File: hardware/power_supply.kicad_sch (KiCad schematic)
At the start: 19 parts, among them U4 LM5164DDA, U5 AP7361-33E

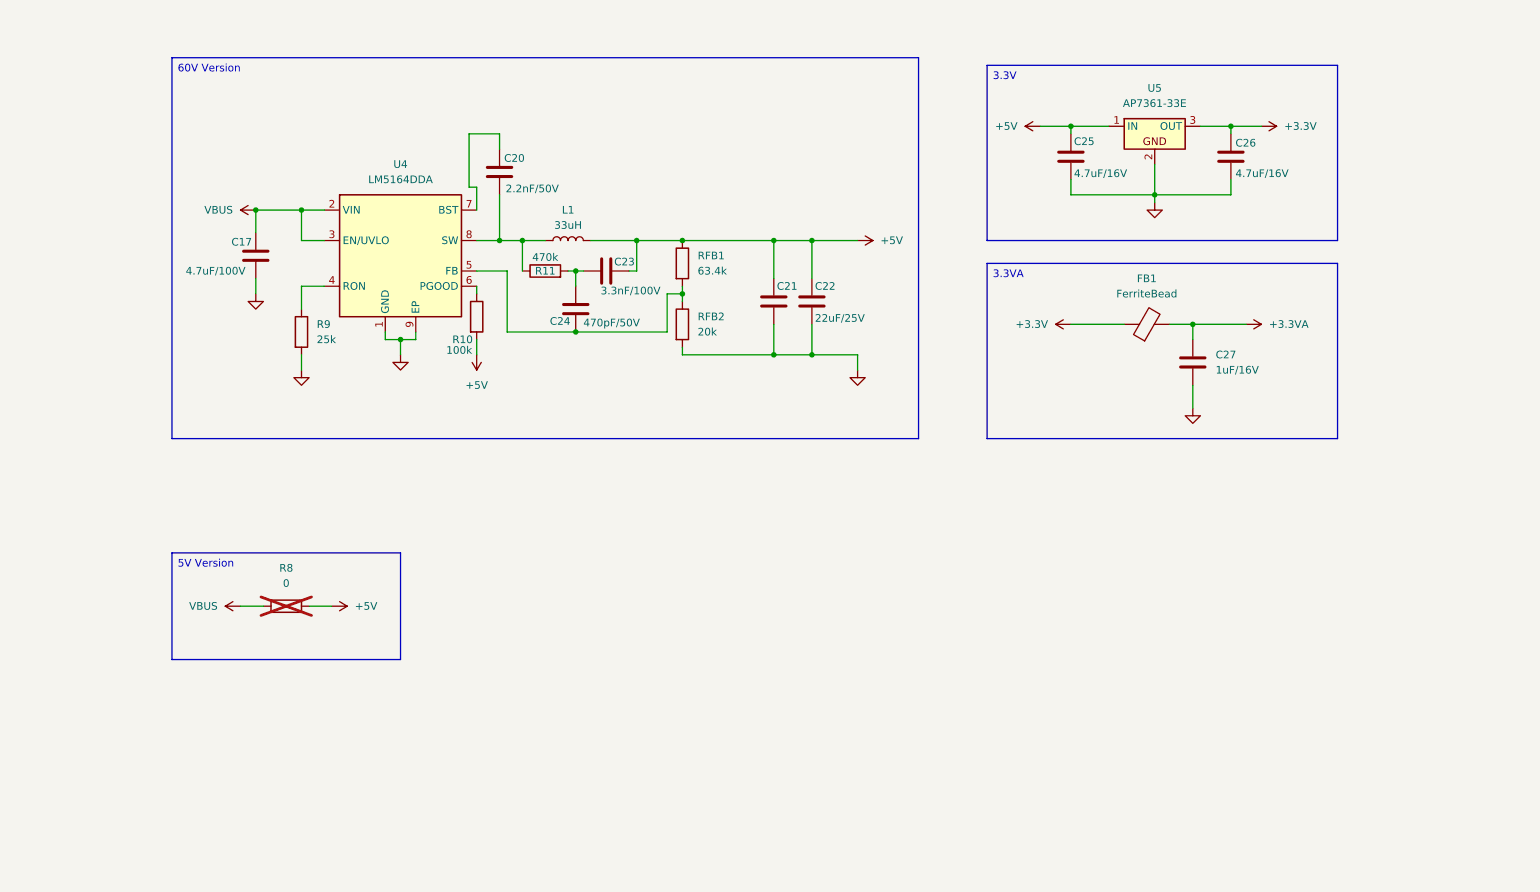
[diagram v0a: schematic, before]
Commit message: ✨ Further power supply schematic
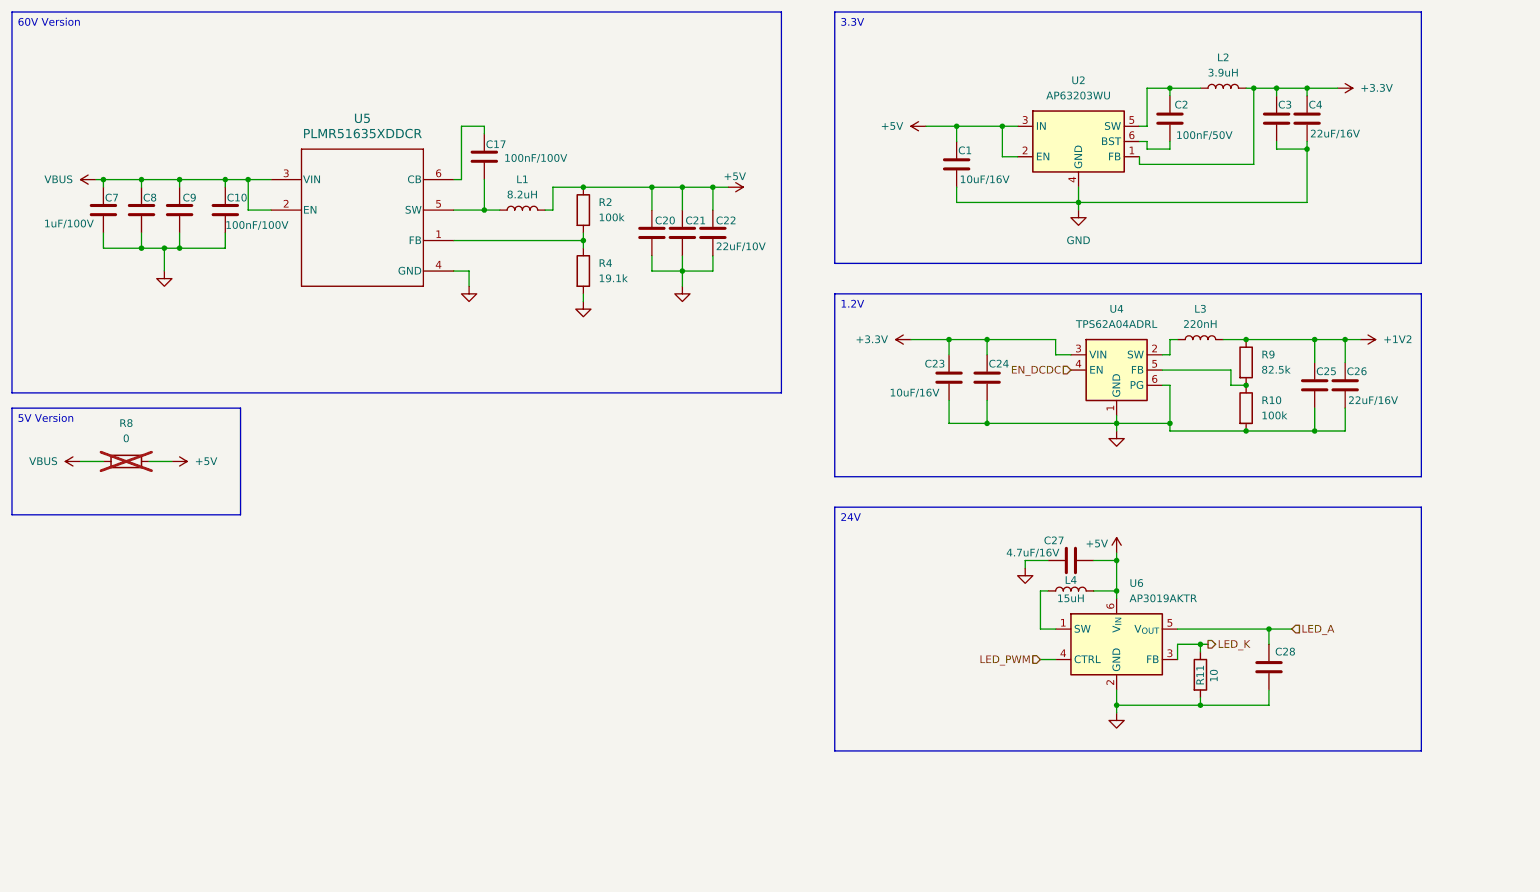
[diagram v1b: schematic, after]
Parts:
- removed FB1: FerriteBead, symbol Device:FerriteBead
- removed RFB1: 63.4k, symbol Device:R
- removed RFB2: 20k, symbol Device:R
- removed U4: LM5164DDA, Package_SO:HSOP-8-1EP_3.9x4.9mm_P1.27mm_EP2.41x3.1mm_ThermalVias, symbol Regulator_Switching:LM5164DDA
- removed U5: AP7361-33E, PCM_Package_TO_SOT_SMD_AKL:SOT-223-3_TabPin2, symbol PCM_Voltage_Regulator_AKL:AP7361-33E
- added C1: 10uF/16V, symbol Device:C
- added C10: 100nF/100V, symbol Device:C
- added C2: 100nF/50V, symbol Device:C
- added C28: 0.22uF/50V, symbol Device:C
- added C3, C4: 22uF/16V, symbol Device:C
- added C7, C8, C9: 1uF/100V, symbol Device:C
- added L2: 3.9uH, symbol Device:L
- added L3: 220nH, symbol Device:L
- added L4: 15uH, symbol Device:L
- added R2: 100k, symbol Device:R
- added R4: 19.1k, symbol Device:R
- added U2: AP63203WU, PCM_Package_TO_SOT_SMD_AKL:TSOT-23-6, symbol Regulator_Switching:AP63203WU
- added U4: TPS62A04ADRL, Package_TO_SOT_SMD:SOT-563, symbol Regulator_Switching:TPS62A01ADRL
- added U5: PLMR51635XDDCR, DDC0006A-MFG, symbol lmr51635:PLMR51635XDDCR
- added U6: AP3019AKTR, Package_TO_SOT_SMD:SOT-23-6, symbol Driver_LED:AP3019AKTR
- C17: value 4.7uF/100V -> 100nF/100V
- C20: value 2.2nF/50V -> C
- C21, C22: value 22uF/25V -> 22uF/10V
- C23: value 3.3nF/100V -> 10uF/16V
- C24: value 470pF/50V -> 4.7nF/16V
- C25, C26: value 4.7uF/16V -> 22uF/16V
- C27: value 1uF/16V -> 4.7uF/16V
- L1: value 33uH -> 8.2uH
- R11: value 470k -> 10
- R9: value 25k -> 82.5k
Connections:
- net +3.3VA is gone; now on net GND: C27.1
- net +3.3V: now also C23.1, C24.1, C3.1, C4.1, L2.2, U2.1 (FB), U4.3 (VIN); no longer C26.1
- net +5V: now also C20.1, C27.2, C1.1, L4.2, R2.1, U2.2 (EN), U2.3 (IN), U6.6 (V_{IN}); no longer C23.2, C25.1, R10.2
- net GND: now also C20.2, C23.2, C24.2, R10.2, R11.2, C1.2, C10.2, C28.2, C3.2, C4.2, C7.2, C8.2, C9.2, R4.2, U2.4 (GND), U4.1 (GND), U4.6 (PG), U5.4 (GND), U6.2 (GND); no longer C17.2, C27.2, R9.2
- net VBUS: now also C10.1, C7.1, C8.1, C9.1, U5.2 (EN), U5.3 (VIN); no longer C17.1
- net +1V2: now reaches R9.1
- net +1V2: now also C25.1, C26.1, L3.2
- net at R10.1: now also R9.2, U4.5 (FB)
- new net: L3.1, U4.2 (SW)
- new net: C2.1, L2.1, U2.5 (SW)
- new net: C2.2, U2.6 (BST)
- new net: R2.2, R4.1, U5.1 (FB)
- new net: C17.2, L1.1, U5.5 (SW)
- new net: L4.1, U6.1 (SW)
- new net: C17.1, U5.6 (CB)
- new net EN_DCDC: U4.4 (EN)
- new net LED_A: C28.1, U6.5 (V_{OUT})
- new net LED_K: R11.1, U6.3 (FB)
- new net LED_PWM: U6.4 (CTRL)
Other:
- moved on the sheet: R8

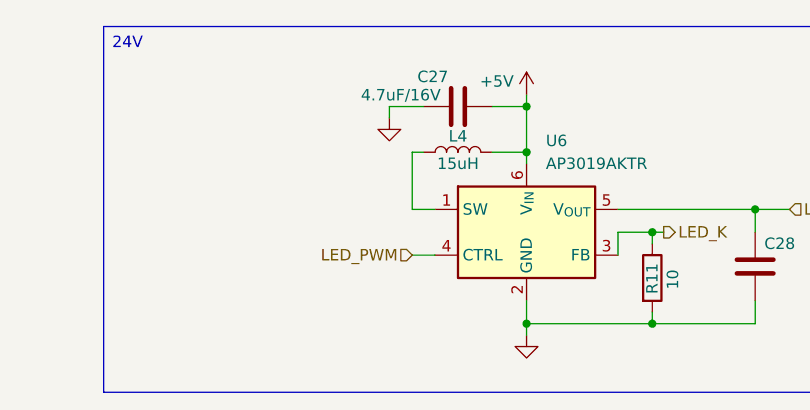
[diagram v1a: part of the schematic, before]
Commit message: ✨ Add pulldown to disable the led by default
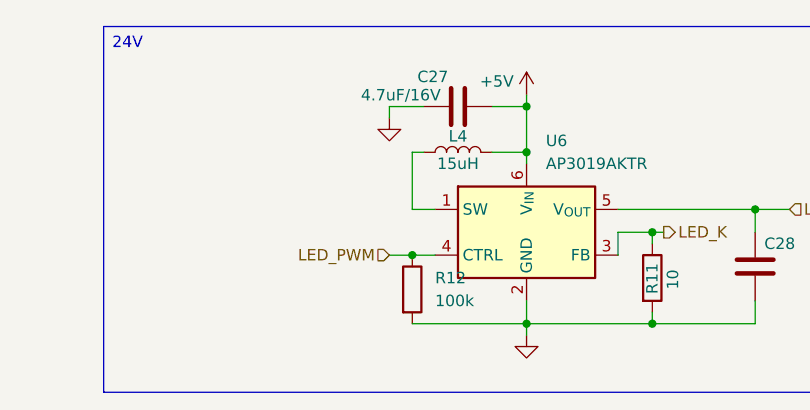
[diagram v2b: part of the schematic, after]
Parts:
- added R12: 100k, symbol Device:R
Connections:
- net GND: now also R12.2
- net LED_PWM: now also R12.1
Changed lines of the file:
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@@
 	)
 	(junction
+		(at 186.69 123.19)
+		(diameter 0)
+		(color 0 0 0 0)
+	)
+	(junction
 		(at 208.28 27.94)
 		(diameter 0)
@@
 	(wire
 		(pts
+			(xy 186.69 130.81) (xy 199.39 130.81)
+		)
+		(stroke
+			(width 0)
+			(type default)
+		)
+	)
+	(wire
+		(pts
 			(xy 110.49 62.23) (xy 110.49 63.5)
 		)
@@
 	(wire
 		(pts
-			(xy 186.69 123.19) (xy 189.23 123.19)
+			(xy 184.15 123.19) (xy 186.69 123.19)
 		)
 		(stroke
@@
 	(wire
 		(pts
+			(xy 186.69 123.19) (xy 189.23 123.19)
+		)
+		(stroke
+			(width 0)
+			(type default)
+		)
+	)
+	(wire
+		(pts
 			(xy 224.79 118.11) (xy 228.6 118.11)
 		)
@@
 	(hierarchical_label "LED_PWM"
 		(shape input)
-		(at 186.69 123.19 180)
+		(at 184.15 123.19 180)
 		(effects
 			(font
@@
 					(unit 1)
 				)
+			)
+		)
+	)
+	(symbol
+		(lib_id "Device:R")
+		(at 186.69 127 0)
+		(unit 1)
+		(exclude_from_sim no)
+		(in_bom yes)
+		(on_board yes)
+		(dnp no)
+		(fields_autoplaced yes)
+		(property "Reference" "R12"
+			(at 189.23 125.7299 0)
+			(effects
+				(font
+					(size 1.27 1.27)
+				)
+				(justify left)
+			)
+		)
+		(property "Value" "100k"
+			(at 189.23 128.2699 0)
+			(effects
+				(font
+					(size 1.27 1.27)
+				)
+				(justify left)
+			)
+		)
+		(property "Footprint" ""
+			(at 184.912 127 90)
+			(effects
+				(font
+					(size 1.27 1.27)
+				)
+				(hide yes)
+			)
+		)
+		(property "Datasheet" "~"
+			(at 186.69 127 0)
+			(effects
+				(font
+					(size 1.27 1.27)
+				)
+				(hide yes)
+			)
+		)
+		(property "Description" "Resistor"
+			(at 186.69 127 0)
+			(effects
+				(font
+					(size 1.27 1.27)
+				)
+				(hide yes)
+			)
+		)
+		(pin "1"
+		)
+		(pin "2"
+		)
+		(instances
+			(project "peak"
+				(path "/54a54a18-4a65-4728-b17a-32b4a97370c1/2f3b67c0-998d-4e44-aea4-3f3ad43237a6"
+					(reference "R12")
+					(unit 1)
+				)

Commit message: ✨ Further schematic updates
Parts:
- removed C27: 4.7uF/16V, symbol Device:C
- removed C28: 0.22uF/50V, symbol Device:C
- removed L4: 15uH, symbol Device:L
- removed R11: 10, symbol Device:R
- removed R12: 100k, symbol Device:R
- removed U6: AP3019AKTR, Package_TO_SOT_SMD:SOT-23-6, symbol Driver_LED:AP3019AKTR
- added C30, C31, C32: 1uF, symbol Device:C
- added C33: 4.7uF, symbol Device:C
- added FB1: FerriteBead, symbol Device:FerriteBead
- added TP1, TP9: 5V, TestPoint:TestPoint_Loop_D2.50mm_Drill1.0mm, symbol Connector:TestPoint
- added TP2: 3.3V, TestPoint:TestPoint_Loop_D2.50mm_Drill1.0mm, symbol Connector:TestPoint
- added TP3: 1.2V, TestPoint:TestPoint_Loop_D2.50mm_Drill1.0mm, symbol Connector:TestPoint
- added TP5: 2.5V, TestPoint:TestPoint_Loop_D2.50mm_Drill1.0mm, symbol Connector:TestPoint
- added TP6: 3.3VA, TestPoint:TestPoint_Loop_D2.50mm_Drill1.0mm, symbol Connector:TestPoint
- added U8: MCP1700T-2502E-TT, PCM_Package_TO_SOT_SMD_AKL:SOT-23, symbol PCM_Voltage_Regulator_AKL:MCP1700T-2502E-TT
- R9: value 82.5k -> 100k
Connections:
- net +1V2: now also TP3.1
- net +3.3V: now also C30.1, C32.1, FB1.1, TP2.1, U8.3 (IN)
- net +5V: now also TP1.1, TP9.1
- net GND: now also C30.2, C31.2, C32.2, C33.2, U8.1
- net FB_DCDC: now reaches R10.1, R9.2, U4.5 (FB)
- new net +2V5: C31.1, TP5.1, U8.2 (OUT)
- new net +3.3VA: C33.1, FB1.2, TP6.1
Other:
- moved on the sheet: R10, R9

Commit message: 📂 PCB updates
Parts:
- removed C10: 100nF/100V, symbol Device:C
- removed TP9: 5V, TestPoint:TestPoint_Loop_D2.50mm_Drill1.0mm, symbol Connector:TestPoint
- C1, C23: value 10uF/16V -> 10uF; footprint (none) -> Capacitor_SMD:C_0805_2012Metric
- C17: footprint (none) -> Capacitor_SMD:C_0805_2012Metric
- C2, C30, C31, C32, C33: footprint (none) -> Capacitor_SMD:C_0603_1608Metric
- C20: value C -> 22uF; footprint (none) -> Capacitor_SMD:C_0805_2012Metric
- C21, C22: value 22uF/10V -> 22uF; footprint (none) -> Capacitor_SMD:C_0805_2012Metric
- C24: value 4.7nF/16V -> 4.7nF; footprint (none) -> Capacitor_SMD:C_0603_1608Metric
- C25, C26, C3, C4: value 22uF/16V -> 22uF; footprint (none) -> Capacitor_SMD:C_0805_2012Metric
- C7, C8, C9: footprint (none) -> Capacitor_SMD:C_1206_3216Metric
- FB1: footprint (none) -> Inductor_SMD:L_0805_2012Metric
- L1: footprint (none) -> Inductor_SMD:L_Bourns_SRP5030T
- L2: footprint (none) -> Inductor_SMD:L_APV_ANR4030
- L3: footprint (none) -> Inductor_SMD:L_0603_1608Metric
- R10, R2, R4, R8, R9: footprint (none) -> Resistor_SMD:R_0603_1608Metric
- TP1, TP2, TP3, TP5, TP6: footprint TestPoint:TestPoint_Loop_D2.50mm_Drill1.0mm -> TestPoint:TestPoint_Pad_D1.0mm
- U5: footprint DDC0006A-MFG -> Package_TO_SOT_SMD:SOT-23-6

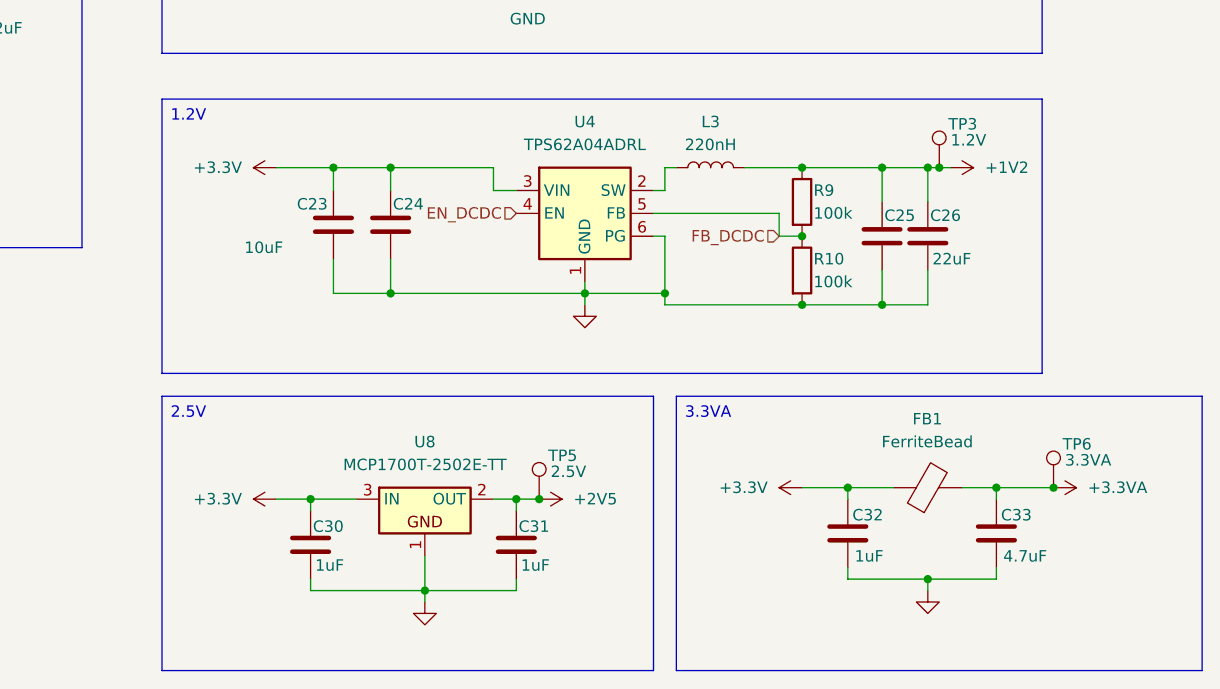
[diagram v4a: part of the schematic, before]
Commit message: 🐛 Fix errors from rev1.0
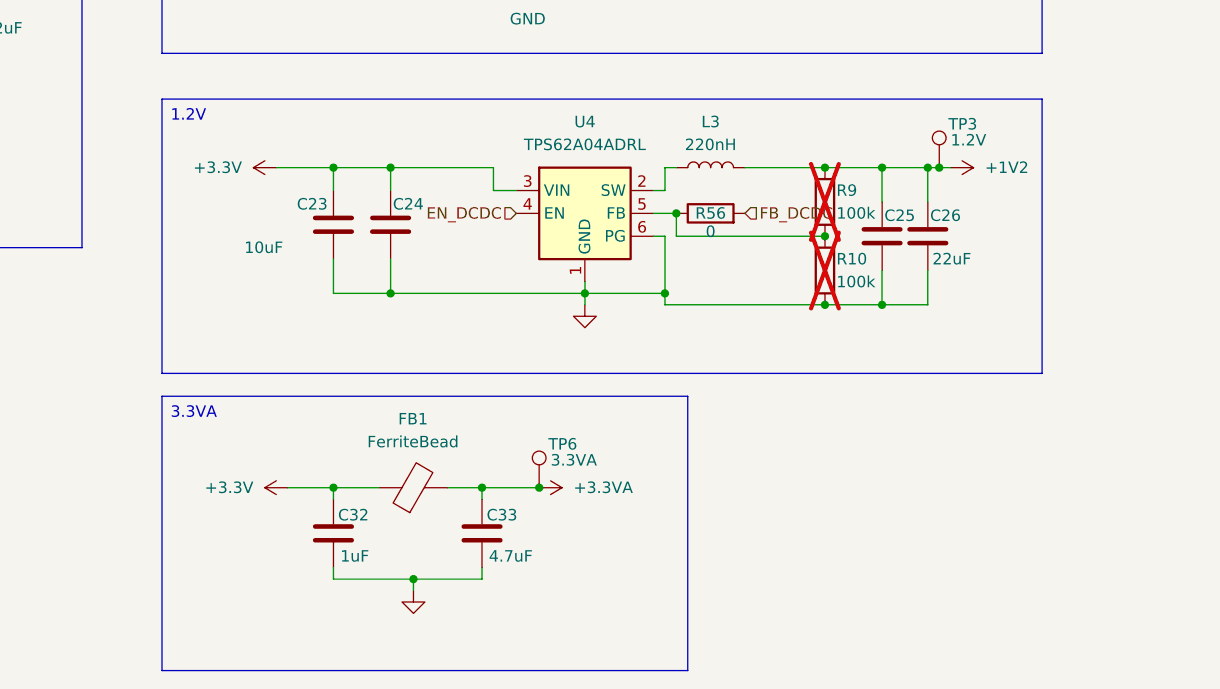
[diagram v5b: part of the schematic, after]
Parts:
- removed C30, C31: 1uF, Capacitor_SMD:C_0603_1608Metric, symbol Device:C
- removed TP5: 2.5V, TestPoint:TestPoint_Pad_D1.0mm, symbol Connector:TestPoint
- removed U8: MCP1700T-2502E-TT, PCM_Package_TO_SOT_SMD_AKL:SOT-23, symbol PCM_Voltage_Regulator_AKL:MCP1700T-2502E-TT
- added R56: 0, PCM_Resistor_SMD_AKL:R_0402_1005Metric, symbol Device:R
- R10, R9: now not fitted
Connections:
- net FB_DCDC: now also R56.2; no longer R10.1, R9.2, U4.5 (FB)
- new net: R10.1, R56.1, R9.2, U4.5 (FB)
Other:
- moved on the sheet: C32, C33, FB1, TP6

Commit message: 🔥 Redo the PCB
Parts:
- removed R56: 0, PCM_Resistor_SMD_AKL:R_0402_1005Metric, symbol Device:R
- added R58: 0, PCM_Resistor_SMD_AKL:R_0402_1005Metric, symbol Device:R
- R10, R9: now fitted
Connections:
- net +3.3V: now also R58.1
- net EN_DCDC: no longer names the net of U4.4 (EN)
- net EN_DCDC: now also R58.2
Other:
- moved on the sheet: L3, U4

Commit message: ✨ Final PCB updates
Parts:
- added C218, C219: 1uF, Capacitor_SMD:C_0603_1608Metric, symbol Device:C
- added R207: 0, Resistor_SMD:R_0402_1005Metric, symbol Device:R
- added U204: LP5910-1.8DRV, PCM_Package_SON_AKL:WSON-6-1EP_2x2mm_P0.65mm_EP1x1.6mm, symbol Regulator_Linear:LP5912-1.8DRV
- renumbered C7 to C201, C8 to C202, C9 to C203, C17 to C204, C20 to C205, C21 to C206, C22 to C207, C1 to C208, C2 to C209, C3 to C210, C4 to C211, C23 to C212, C24 to C213, C25 to C214, C26 to C215, C32 to C216, C33 to C217, FB1 to FB201, L1 to L201, L2 to L202, L3 to L203, R2 to R201, R4 to R202, R8 to R203, R58 to R204, R9 to R205, R10 to R206, TP1 to TP201, TP2 to TP202, TP3 to TP203, TP6 to TP204, U5 to U201, U2 to U202, U4 to U203
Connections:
- net +3.3V: now also C218.1, R207.1, U204.4 (EN), U204.6 (IN)
- net GND: now also C218.2, C219.2, U204.3 (PG), U204.5 (GND), U204.7 (EP)
- new net +1V8: C219.1, R207.2, U204.1 (OUT)

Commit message: ✨ Final PCB v.1 updates
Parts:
- removed U203: TPS62A04ADRL, Package_TO_SOT_SMD:SOT-563, symbol Regulator_Switching:TPS62A01ADRL
- added R208, R209: 0, PCM_Resistor_SMD_AKL:R_0402_1005Metric, symbol Device:R
- added U203: TLV62569DRL, Package_TO_SOT_SMD:SOT-563, symbol Regulator_Switching:TLV62569DRL
- L203: value 220nH -> 2.2uH; footprint Inductor_SMD:L_0603_1608Metric -> PCM_Inductor_SMD_AKL:L_1008_2520Metric
- R204: now not fitted
- R205, R206: footprint Resistor_SMD:R_0603_1608Metric -> PCM_Resistor_SMD_AKL:R_0402_1005Metric; now not fitted
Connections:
- net +3.3V: now also U203.3 (VIN)
- net GND: now also U203.2 (GND)
- net at R204.2: now also R208.2, U203.5 (EN)
- net at L203.1: now also U203.4 (SW)
- net at R205.2, R206.1: now also R209.1, U203.1 (FB)
- new net EN_DCDC: R208.1
- new net FB_DCDC: R209.2
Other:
- moved on the sheet: C214, C215, L203, TP203
